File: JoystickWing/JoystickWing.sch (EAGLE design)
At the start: 23 parts, among them J1 5747844-4, Q1 2N2222

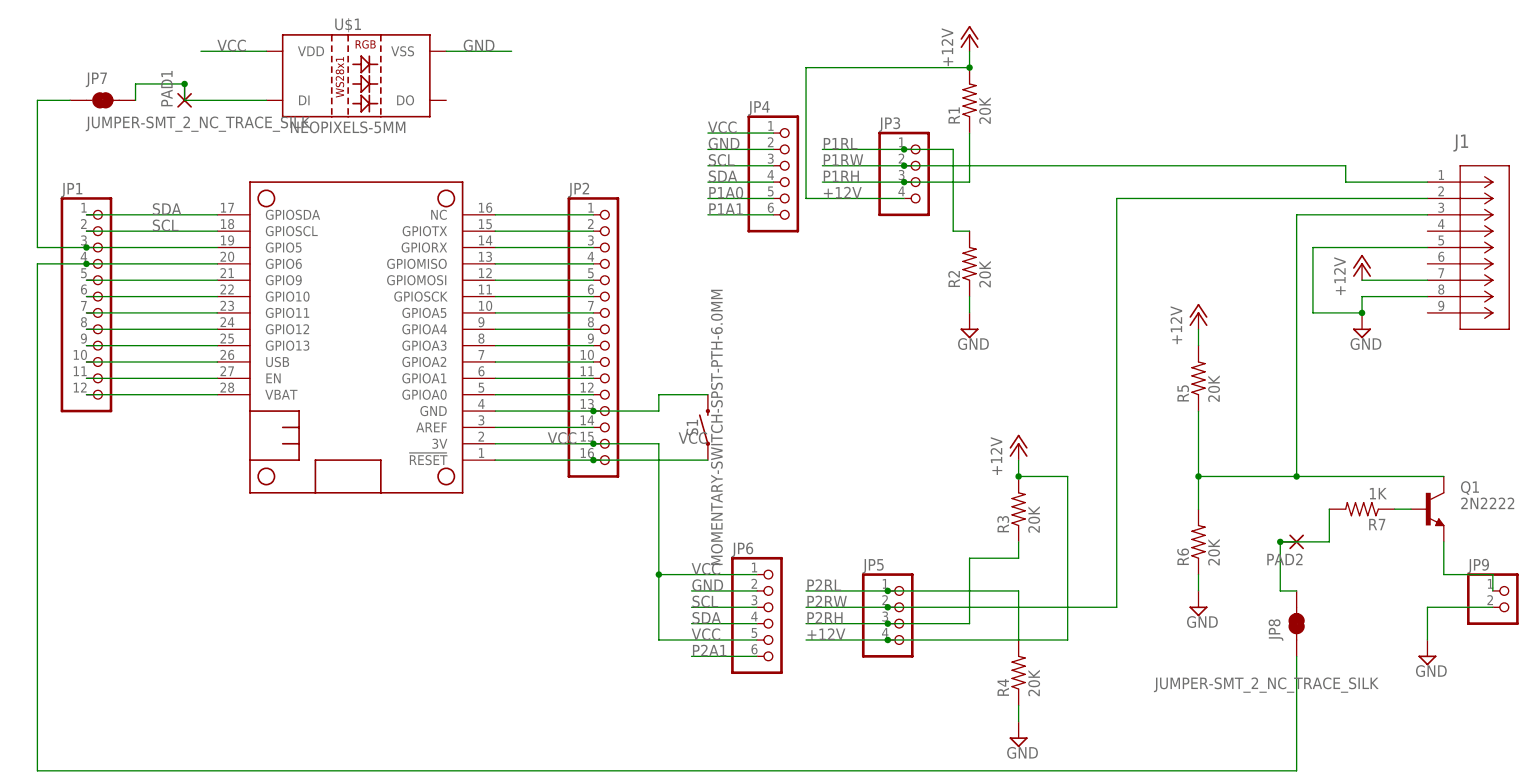
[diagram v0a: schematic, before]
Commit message: Removed transistor
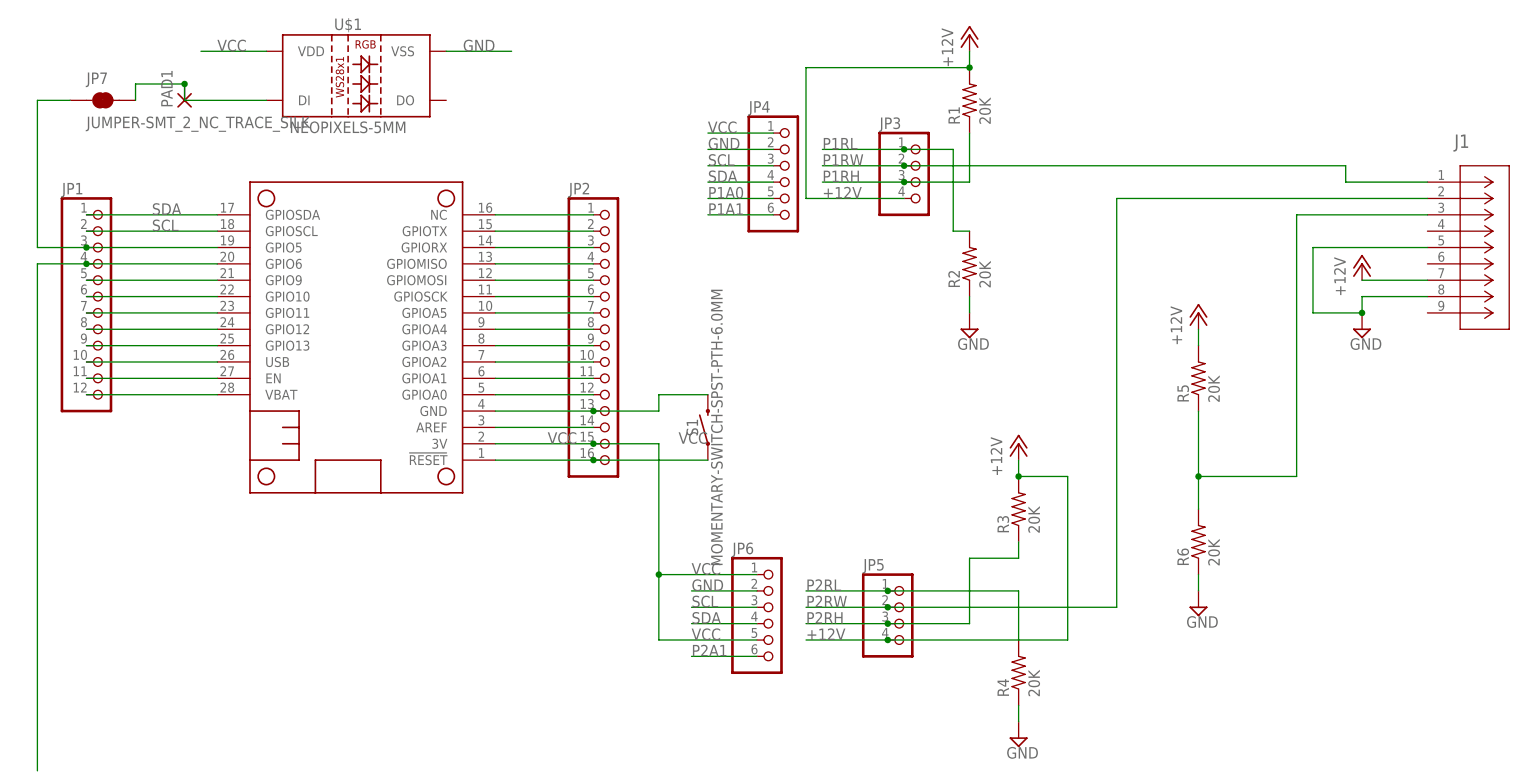
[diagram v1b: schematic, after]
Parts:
- removed JP8: JUMPER-SMT_2_NC_TRACE_SILK, SparkFun-Jumpers:JUMPER-SMT_2_NC_TRACE_SILK
- removed JP9: (no value), pinhead:PINHD-1X2
- removed PAD2: (no value), wirepad:2,54/1,1
- removed Q1: 2N2222, adafruit:2N2222
- removed R7: 1K, adafruit:R-US_0204/7
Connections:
- removed net N$26: Q1.B, R7.1
- removed net N$27: JP9.1, Q1.E
- removed net N$28: JP8.2, PAD2.P, R7.2
- net GND: no longer JP9.2
- net N$2: no longer JP8.1
- net N$7: no longer Q1.C

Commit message: Update with address pads
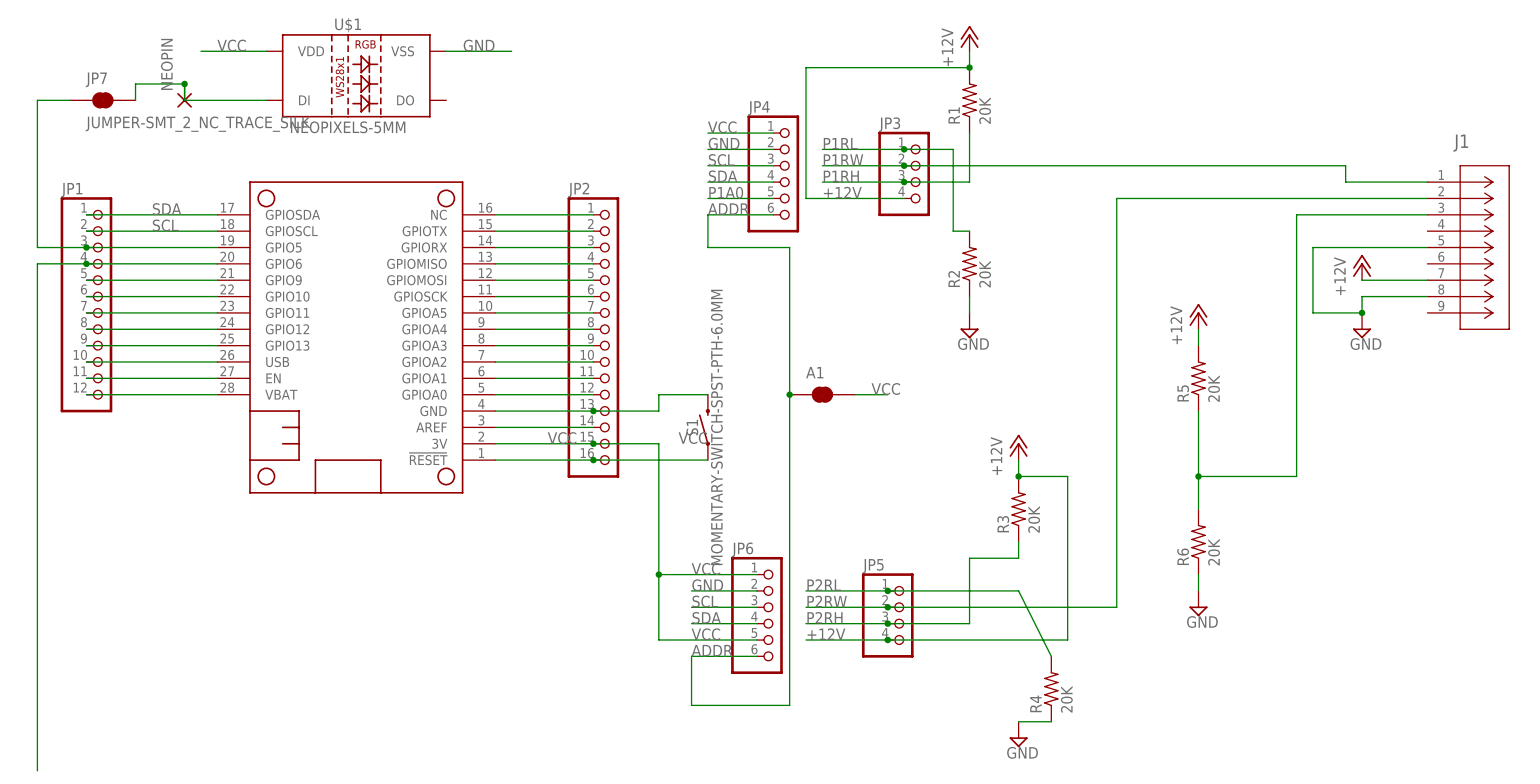
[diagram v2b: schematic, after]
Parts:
- added A1: JUMPER-SMT_2_NC_TRACE_SILK, SparkFun-Jumpers:JUMPER-SMT_2_NC_TRACE_SILK
- renumbered PAD1 to NEOPIN
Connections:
- removed net P1A1: JP4.6
- removed net P2A1: JP6.6
- new net ADDR: A1.1, JP4.6, JP6.6
- net VCC: now also A1.2
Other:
- moved on the sheet: R4
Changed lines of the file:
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@@
 <part name="U$1" library="milador" deviceset="NEOPIXELS-5MM" device="" package3d_urn="urn:adsk.eagle:package:6677832/4"/>
 <part name="JP7" library="SparkFun-Jumpers" deviceset="JUMPER-SMT_2_NC_TRACE" device="_SILK"/>
-<part name="PAD1" library="wirepad" library_urn="urn:adsk.eagle:library:412" deviceset="2,54/1,1" device="" package3d_urn="urn:adsk.eagle:package:30836/1"/>
+<part name="NEOPIN" library="wirepad" library_urn="urn:adsk.eagle:library:412" deviceset="2,54/1,1" device="" package3d_urn="urn:adsk.eagle:package:30836/1"/>
 <part name="S1" library="SparkFun-Switches" library_urn="urn:adsk.eagle:library:535" deviceset="MOMENTARY-SWITCH-SPST" device="-PTH-6.0MM" package3d_urn="urn:adsk.eagle:package:40163/1"/>
+<part name="A1" library="SparkFun-Jumpers" deviceset="JUMPER-SMT_2_NC_TRACE" device="_SILK"/>
 </parts>
 <sheets>
@@
 <attribute name="VALUE" x="28.702" y="19.05" size="1.778" layer="96" rot="R90"/>
 </instance>
-<instance part="R4" gate="G$1" x="25.4" y="-2.54" smashed="yes" rot="R90">
-<attribute name="NAME" x="23.9014" y="-6.35" size="1.778" layer="95" rot="R90"/>
-<attribute name="VALUE" x="28.702" y="-6.35" size="1.778" layer="96" rot="R90"/>
+<instance part="R4" gate="G$1" x="30.48" y="-5.08" smashed="yes" rot="R90">
+<attribute name="NAME" x="28.9814" y="-8.89" size="1.778" layer="95" rot="R90"/>
+<attribute name="VALUE" x="33.782" y="-8.89" size="1.778" layer="96" rot="R90"/>
 </instance>
 <instance part="SUPPLY4" gate="GND" x="53.34" y="7.62" smashed="yes">
@@
 <attribute name="VALUE" x="-119.38" y="83.82" size="1.778" layer="96" font="vector" align="top-left"/>
 </instance>
-<instance part="PAD1" gate="1" x="-104.14" y="86.36" smashed="yes" rot="R90">
-<attribute name="NAME" x="-105.9942" y="85.217" size="1.778" layer="95" rot="R90"/>
+<instance part="NEOPIN" gate="1" x="-104.14" y="86.36" smashed="yes" rot="R90">
+<attribute name="NAME" x="-105.9942" y="87.757" size="1.778" layer="95" rot="R90"/>
 <attribute name="VALUE" x="-100.838" y="85.217" size="1.778" layer="96" rot="R90"/>
 </instance>
@@
 <attribute name="NAME" x="-24.384" y="35.56" size="1.778" layer="95" font="vector" rot="R90" align="bottom-center"/>
 <attribute name="VALUE" x="-22.352" y="35.56" size="1.778" layer="96" font="vector" rot="R90" align="top-center"/>
+</instance>
+<instance part="A1" gate="G$1" x="-5.08" y="40.64" smashed="yes">
+<attribute name="NAME" x="-7.62" y="43.18" size="1.778" layer="95" font="vector"/>
 </instance>
 </instances>
@@
 <pinref part="R4" gate="G$1" pin="1"/>
 <pinref part="SUPPLY3" gate="GND" pin="GND"/>
-<wire x1="25.4" y1="-7.62" x2="25.4" y2="-10.16" width="0.1524" layer="91"/>
+<wire x1="30.48" y1="-10.16" x2="25.4" y2="-10.16" width="0.1524" layer="91"/>
 </segment>
 <segment>
@@
 <label x="-99.06" y="93.98" size="1.778" layer="95"/>
 </segment>
+<segment>
+<pinref part="A1" gate="G$1" pin="2"/>
+<wire x1="0" y1="40.64" x2="5.08" y2="40.64" width="0.1524" layer="91"/>
+<label x="2.54" y="40.64" size="1.778" layer="95"/>
+</segment>
 </net>
 <net name="P1A0" class="0">
@@
 <wire x1="-12.7" y1="71.12" x2="-22.86" y2="71.12" width="0.1524" layer="91"/>
 <label x="-22.86" y="71.12" size="1.778" layer="95"/>
-</segment>
-</net>
-<net name="P1A1" class="0">
-<segment>
-<pinref part="JP4" gate="A" pin="6"/>
-<wire x1="-12.7" y1="68.58" x2="-22.86" y2="68.58" width="0.1524" layer="91"/>
-<label x="-22.86" y="68.58" size="1.778" layer="95"/>
 </segment>
 </net>
@@
 </segment>
 </net>
-<net name="P2A1" class="0">
+<net name="ADDR" class="0">
 <segment>
 <pinref part="JP6" gate="A" pin="6"/>
 <wire x1="-15.24" y1="0" x2="-25.4" y2="0" width="0.1524" layer="91"/>
 <label x="-25.4" y="0" size="1.778" layer="95"/>
+<wire x1="-25.4" y1="0" x2="-25.4" y2="-7.62" width="0.1524" layer="91"/>
+<wire x1="-25.4" y1="-7.62" x2="-10.16" y2="-7.62" width="0.1524" layer="91"/>
+<pinref part="A1" gate="G$1" pin="1"/>
+<wire x1="-10.16" y1="-7.62" x2="-10.16" y2="40.64" width="0.1524" layer="91"/>
+<wire x1="-10.16" y1="40.64" x2="-10.16" y2="63.5" width="0.1524" layer="91"/>
+<junction x="-10.16" y="40.64"/>
+<wire x1="-10.16" y1="63.5" x2="-22.86" y2="63.5" width="0.1524" layer="91"/>
+<pinref part="JP4" gate="A" pin="6"/>
+<wire x1="-12.7" y1="68.58" x2="-22.86" y2="68.58" width="0.1524" layer="91"/>
+<label x="-22.86" y="68.58" size="1.778" layer="95"/>
+<wire x1="-22.86" y1="63.5" x2="-22.86" y2="68.58" width="0.1524" layer="91"/>
 </segment>
 </net>
@@
 <pinref part="R4" gate="G$1" pin="2"/>
 <wire x1="5.08" y1="10.16" x2="25.4" y2="10.16" width="0.1524" layer="91"/>
-<wire x1="25.4" y1="10.16" x2="25.4" y2="2.54" width="0.1524" layer="91"/>
+<wire x1="25.4" y1="10.16" x2="30.48" y2="0" width="0.1524" layer="91"/>
 </segment>
 </net>
@@
 <segment>
 <pinref part="U$1" gate="G$1" pin="DI"/>
-<pinref part="PAD1" gate="1" pin="P"/>
+<pinref part="NEOPIN" gate="1" pin="P"/>
 <wire x1="-91.44" y1="86.36" x2="-104.14" y2="86.36" width="0.1524" layer="91"/>
 <wire x1="-104.14" y1="86.36" x2="-104.14" y2="88.9" width="0.1524" layer="91"/>
